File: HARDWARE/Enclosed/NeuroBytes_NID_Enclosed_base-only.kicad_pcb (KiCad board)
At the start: 2 copper layers, 40.6 x 72.2 mm, 74 parts, among them J1 CONN_01X05, J2 Conn_01x03, J3 USB_OTG, J4 Conn_01x03_Female, J5 Conn_01x03, J6 Conn_01x03_Female, J7 Conn_01x03, J8 Conn_01x03_Female, Q1 MMBT3904, Q2 2N7002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

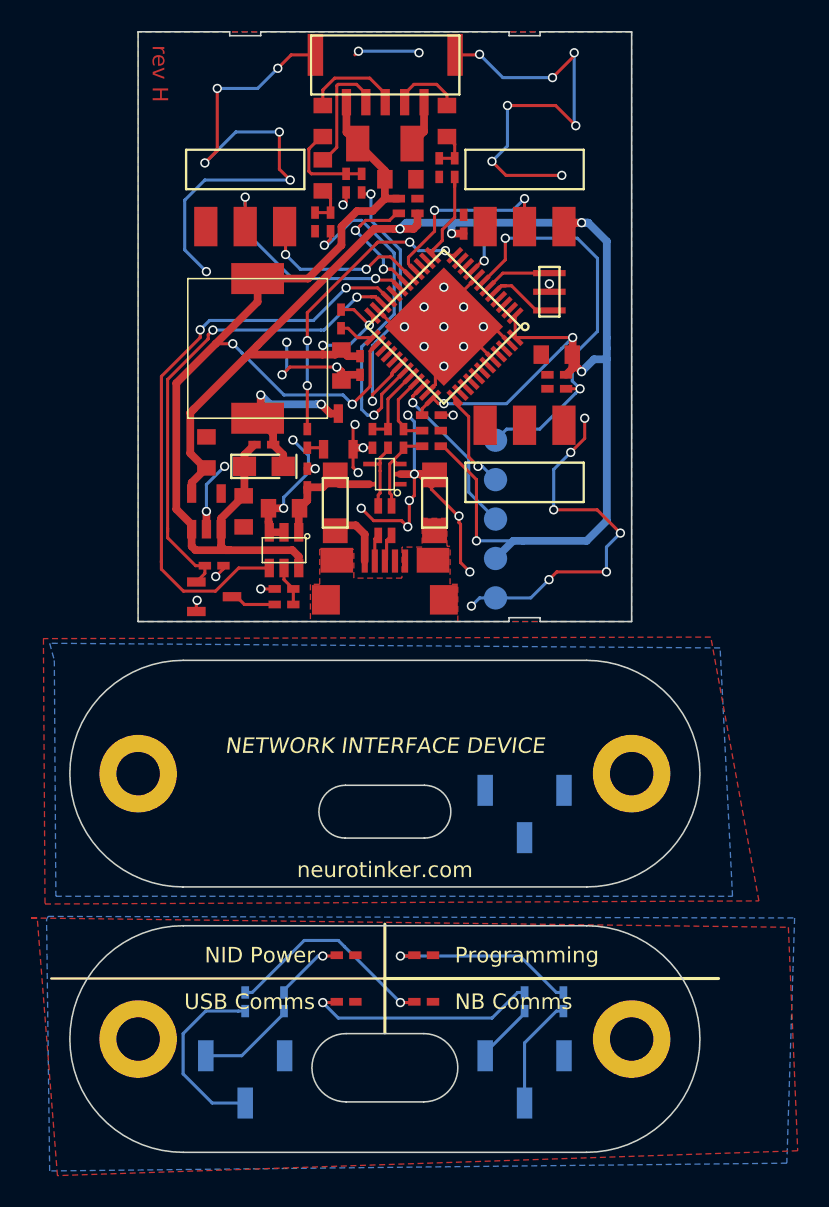
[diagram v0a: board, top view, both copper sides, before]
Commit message: added filtering to NeuroBytes network connection. updated USB ferrites and resonator footprints.
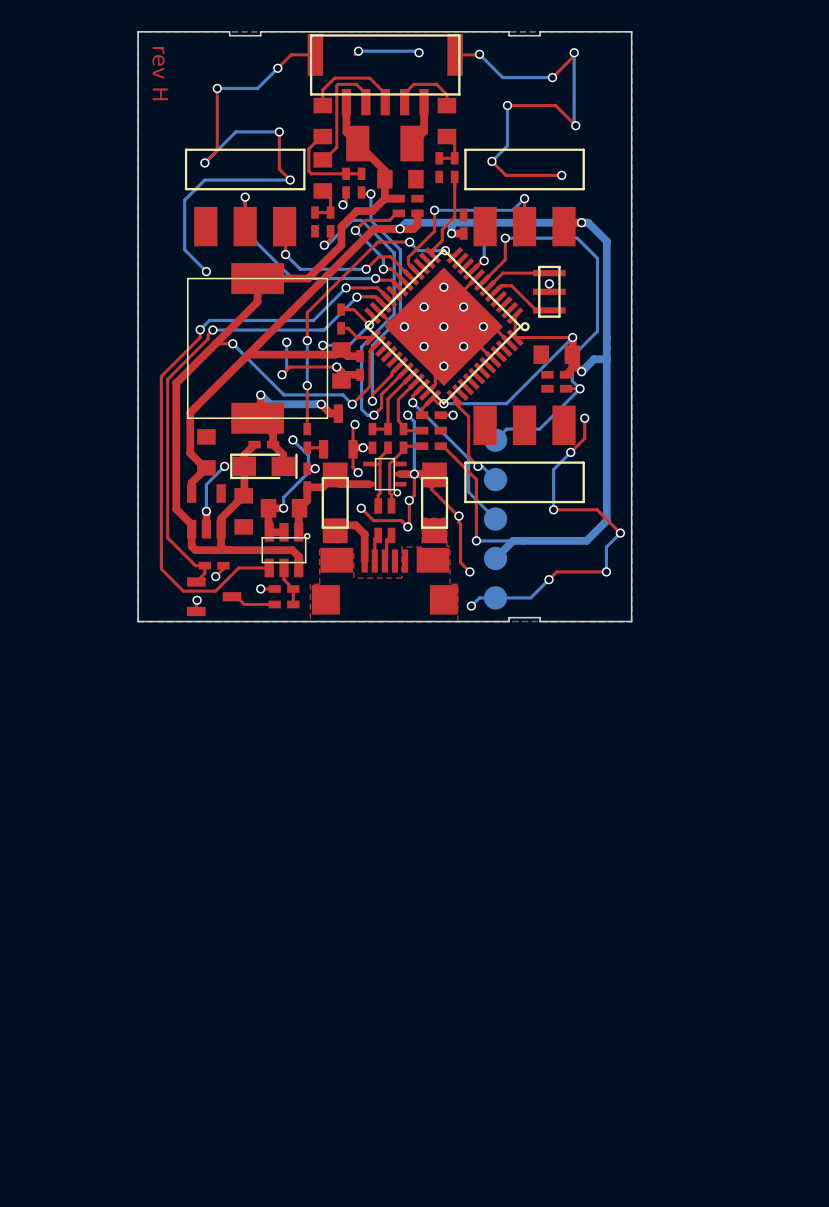
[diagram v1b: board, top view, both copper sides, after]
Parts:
- removed D1: LED_POWER, KiCad_Footprints:ZF_SMD_NonPol_0402
- removed D2: LED_NB, KiCad_Footprints:ZF_SMD_NonPol_0402
- removed D3: LED_USB, KiCad_Footprints:ZF_SMD_NonPol_0402
- removed D4: LED_PROG, KiCad_Footprints:ZF_SMD_NonPol_0402
- removed the G*** at (37.3, 92.5)
- removed J4, J6, J8: Conn_01x03_Female, KiCad_Footprints:ZF_CONN_FHDR_SMD_3
- removed R11, R12, R13, R14: R, KiCad_Footprints:ZF_SMD_NonPol_0402
- removed REF** (x4): ZF_STRUCT_M2-6-hole, KiCad_Footprints:ZF_STRUCT_M2-6-hole
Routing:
- net Net-(D3-Pad2): track 15.0 -> 0.00 mm, vias 1 -> 0
- net Net-(D2-Pad2): track 14.0 -> 0.00 mm, vias 1 -> 0
- net Net-(D4-Pad2): track 12.4 -> 0.00 mm, vias 1 -> 0
- net Net-(J4-Pad2): track 12.0 -> 0.00 mm
- net Net-(J6-Pad2): track 7.22 -> 0.00 mm
- net Net-(J4-Pad3): track 6.32 -> 0.00 mm
- net Net-(D1-Pad2): track 4.48 -> 0.00 mm, vias 1 -> 0
- net Net-(J6-Pad3): track 3.93 -> 0.00 mm
- removed copper zone on B.Cu, net /GND_BACK
- removed copper zone on F.Cu, net /GND_BACK
- removed copper zone on B.Cu, net /GND_FRONT
- removed copper zone on F.Cu, net /GND_FRONT
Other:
- board size 40.6 x 72.2 mm -> 31.8 x 38 mm
- board text removed: "NB Comms"
- board text removed: "NETWORK INTERFACE DEVICE"
- board text removed: "NID Power"
- board text removed: "NeuroBytes"
- board text removed: "Programming"
- board text removed: "To NB Network"
- board text removed: "USB Comms"
- board text removed: "neurotinker.com"
- board text removed: "®"
